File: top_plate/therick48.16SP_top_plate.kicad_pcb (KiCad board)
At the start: 2 copper layers, 313.1 x 75.2 mm, 85 parts, among them U1 HOLE, U10 HOLE, U11 HOLE, U12 HOLE, U13 HOLE, U14 HOLE, U15 HOLE, U16 HOLE, U17 HOLE, U18 HOLE, U19 HOLE, U2 HOLE, U20 HOLE, U21 HOLE, U22 HOLE, U23 HOLE, U24 HOLE, U25 HOLE, U26 HOLE, U27 HOLE, U28 HOLE, U29 HOLE, U3 HOLE, U30 HOLE, U31 HOLE, U32 HOLE, U33 HOLE, U34 HOLE, U35 HOLE, U36 HOLE, U37 HOLE, U38 HOLE, U39 HOLE, U4 HOLE, U40 HOLE, U41 HOLE, U42 HOLE, U43 HOLE, U44 HOLE, U45 HOLE, U46 HOLE, U47 HOLE, U48 HOLE, U49 HOLE, U5 HOLE, U50 HOLE, U51 HOLE, U52 HOLE, U53 HOLE, U54 HOLE, U55 HOLE, U56 HOLE, U57 HOLE, U58 HOLE, U59 HOLE, U6 HOLE, U60 HOLE, U61 HOLE, U62 HOLE, U63 HOLE, U64 HOLE, U65 HOLE, U66 HOLE, U67 HOLE, U7 HOLE, U8 HOLE, U9 HOLE

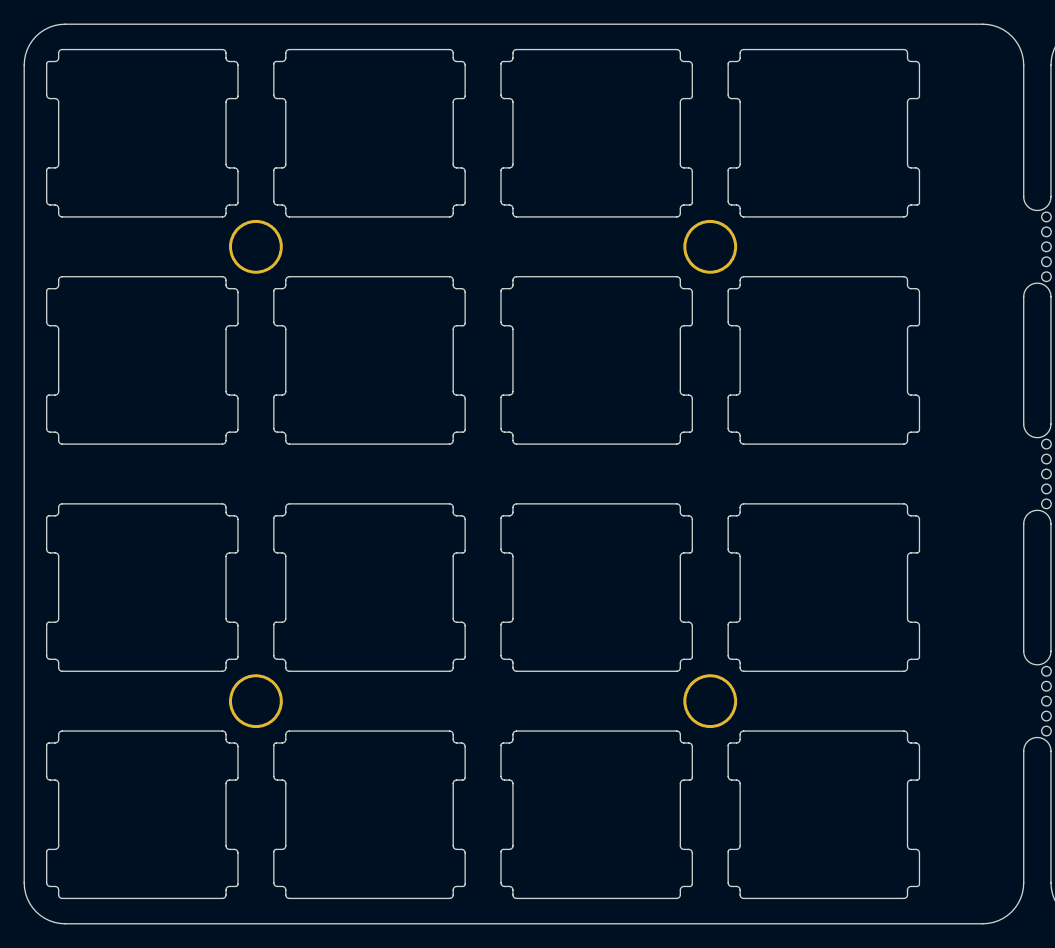
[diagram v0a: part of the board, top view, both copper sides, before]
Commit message: Changed gap between 4X12 and 4X4 to .25 inches
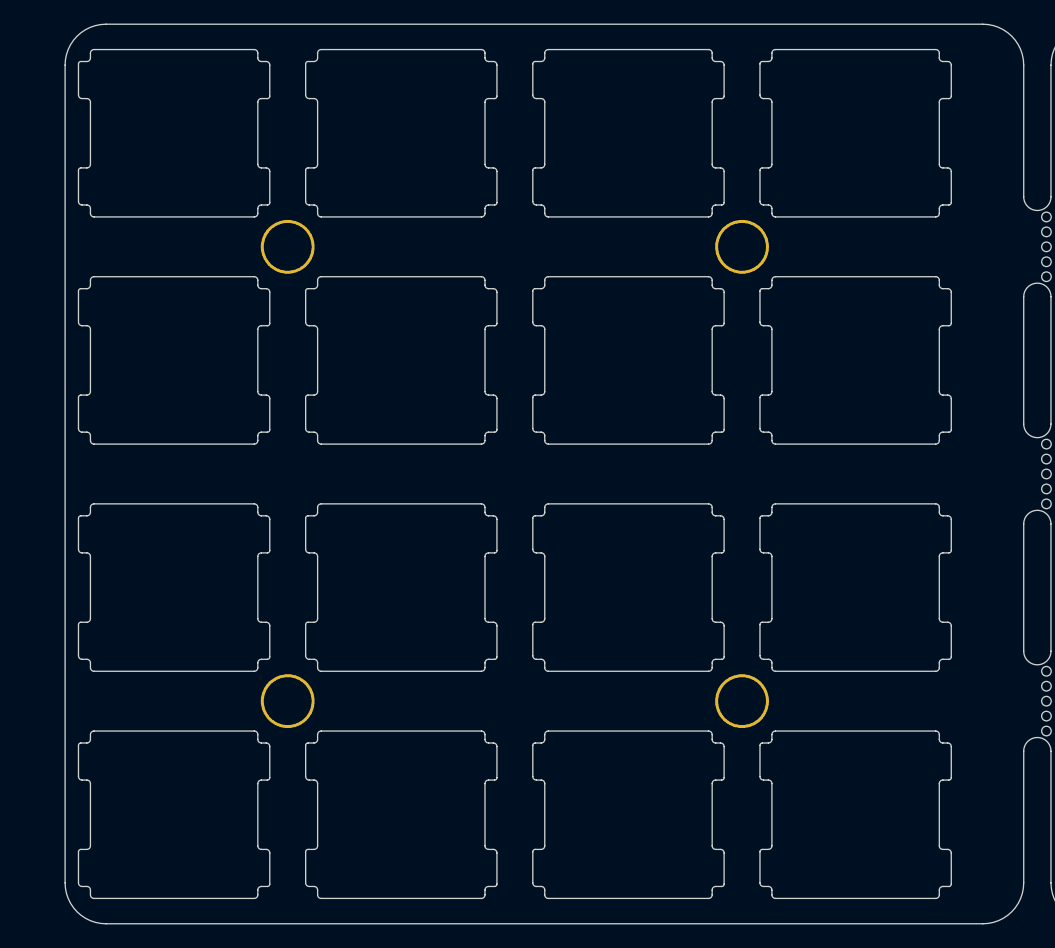
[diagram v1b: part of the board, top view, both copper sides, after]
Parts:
- moved H10 2.66 mm to (105.6, 101.2)
- moved H7 2.66 mm to (67.6, 63.2)
- moved H8 2.66 mm to (105.6, 63.2)
- moved H9 2.66 mm to (67.6, 101.2)
- moved U49 2.66 mm to (58.1, 51.7)
- moved U50 2.66 mm to (77.1, 51.7)
- moved U51 2.66 mm to (96.1, 51.7)
- moved U52 2.66 mm to (115.1, 51.7)
- moved U53 2.66 mm to (58.1, 70.7)
- moved U54 2.66 mm to (77.1, 70.7)
- moved U55 2.66 mm to (96.1, 70.7)
- moved U56 2.66 mm to (115.1, 70.7)
- moved U57 2.66 mm to (58.1, 89.7)
- moved U58 2.66 mm to (77.1, 89.7)
- moved U59 2.66 mm to (96.1, 89.7)
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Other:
- board size 313.1 x 75.2 mm -> 309.7 x 75.2 mm
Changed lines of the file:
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@@
   (general
     (thickness 1.6)
-    (drawings 30)
+    (drawings 31)
     (tracks 0)
     (zones 0)
@@
   )
   (module random-keyboard-parts:plate_hole_4mm_tht locked (layer F.Cu)
-    (at 102.9292 101.212)
+    (at 105.589193 101.212)
     (fp_text reference H10 (at 0.381 1.4097) (layer Dwgs.User)
       (effects (font (size 1 1) (thickness 0.15)))
@@
   )
   (module random-keyboard-parts:plate_hole_4mm_tht locked (layer F.Cu)
-    (at 64.9292 101.212)
+    (at 67.589193 101.212)
     (fp_text reference H9 (at 0.381 1.4097) (layer Dwgs.User)
       (effects (font (size 1 1) (thickness 0.15)))
@@
   )
   (module random-keyboard-parts:plate_hole_4mm_tht locked (layer F.Cu)
-    (at 102.9292 63.212)
+    (at 105.589193 63.212)
     (fp_text reference H8 (at 0.381 1.4097) (layer Dwgs.User)
       (effects (font (size 1 1) (thickness 0.15)))
@@
   )
   (module random-keyboard-parts:plate_hole_4mm_tht locked (layer F.Cu)
-    (at 64.9292 63.212)
+    (at 67.589193 63.212)
     (fp_text reference H7 (at 0.381 1.4097) (layer Dwgs.User)
       (effects (font (size 1 1) (thickness 0.15)))
@@
   )
   (module random-keyboard-parts:MX100_slot (layer F.Cu)
-    (at 112.479704 108.679714)
+    (at 115.139697 108.679714)
     (fp_text reference U64 (at 0.0127 1.8288) (layer Dwgs.User)
       (effects (font (size 1 1) (thickness 0.15)))
@@
   )
   (module random-keyboard-parts:MX100_slot (layer F.Cu)
-    (at 93.479754 108.679714)
+    (at 96.139747 108.679714)
     (fp_text reference U63 (at 0.0127 1.8288) (layer Dwgs.User)
       (effects (font (size 1 1) (thickness 0.15)))
@@
   )
   (module random-keyboard-parts:MX100_slot (layer F.Cu)
-    (at 74.479804 108.679714)
+    (at 77.139797 108.679714)
     (fp_text reference U62 (at 0.0127 1.8288) (layer Dwgs.User)
       (effects (font (size 1 1) (thickness 0.15)))
@@
   )
   (module random-keyboard-parts:MX100_slot (layer F.Cu)
-    (at 55.479854 108.679714)
+    (at 58.139847 108.679714)
     (fp_text reference U61 (at 0.0127 1.8288) (layer Dwgs.User)
       (effects (font (size 1 1) (thickness 0.15)))
@@
   )
   (module random-keyboard-parts:MX100_slot (layer F.Cu)
-    (at 112.479704 89.679764)
+    (at 115.139697 89.679764)
     (fp_text reference U60 (at 0.0127 1.8288) (layer Dwgs.User)
       (effects (font (size 1 1) (thickness 0.15)))
@@
   )
   (module random-keyboard-parts:MX100_slot (layer F.Cu)
-    (at 93.479754 89.679764)
+    (at 96.139747 89.679764)
     (fp_text reference U59 (at 0.0127 1.8288) (layer Dwgs.User)
       (effects (font (size 1 1) (thickness 0.15)))
@@
   )
   (module random-keyboard-parts:MX100_slot (layer F.Cu)
-    (at 74.479804 89.679764)
+    (at 77.139797 89.679764)
     (fp_text reference U58 (at 0.0127 1.8288) (layer Dwgs.User)
       (effects (font (size 1 1) (thickness 0.15)))
@@
   )
   (module random-keyboard-parts:MX100_slot (layer F.Cu)
-    (at 55.479854 89.679764)
+    (at 58.139847 89.679764)
     (fp_text reference U57 (at 0.0127 1.8288) (layer Dwgs.User)
       (effects (font (size 1 1) (thickness 0.15)))
@@
   )
   (module random-keyboard-parts:MX100_slot (layer F.Cu)
-    (at 112.479704 70.679814)
+    (at 115.139697 70.679814)
     (fp_text reference U56 (at 0.0127 1.8288) (layer Dwgs.User)
       (effects (font (size 1 1) (thickness 0.15)))
@@
   )
   (module random-keyboard-parts:MX100_slot (layer F.Cu)
-    (at 93.479754 70.679814)
+    (at 96.139747 70.679814)
     (fp_text reference U55 (at 0.0127 1.8288) (layer Dwgs.User)
       (effects (font (size 1 1) (thickness 0.15)))
@@
   )
   (module random-keyboard-parts:MX100_slot (layer F.Cu)
-    (at 74.479804 70.679814)
+    (at 77.139797 70.679814)
     (fp_text reference U54 (at 0.0127 1.8288) (layer Dwgs.User)
       (effects (font (size 1 1) (thickness 0.15)))
@@
   )
   (module random-keyboard-parts:MX100_slot (layer F.Cu)
-    (at 55.479854 70.679814)
+    (at 58.139847 70.679814)
     (fp_text reference U53 (at 0.0127 1.8288) (layer Dwgs.User)
       (effects (font (size 1 1) (thickness 0.15)))
@@
   )
   (module random-keyboard-parts:MX100_slot (layer F.Cu)
-    (at 112.479704 51.679864)
+    (at 115.139697 51.679864)
     (fp_text reference U52 (at 0.0127 1.8288) (layer Dwgs.User)
       (effects (font (size 1 1) (thickness 0.15)))
@@
   )
   (module random-keyboard-parts:MX100_slot (layer F.Cu)
-    (at 93.479754 51.679864)
+    (at 96.139747 51.679864)
     (fp_text reference U51 (at 0.0127 1.8288) (layer Dwgs.User)
       (effects (font (size 1 1) (thickness 0.15)))
@@
   )
   (module random-keyboard-parts:MX100_slot (layer F.Cu)
-    (at 74.479804 51.679864)
+    (at 77.139797 51.679864)
     (fp_text reference U50 (at 0.0127 1.8288) (layer Dwgs.User)
       (effects (font (size 1 1) (thickness 0.15)))
@@
   )
   (module random-keyboard-parts:MX100_slot (layer F.Cu)
-    (at 55.479854 51.679864)
+    (at 58.139847 51.679864)
     (fp_text reference U49 (at 0.0127 1.8288) (layer Dwgs.User)
       (effects (font (size 1 1) (thickness 0.15)))
@@
     (fp_arc (start -7.8 -5.8) (end -7.8 -6) (angle -90) (layer Edge.Cuts) (width 0.1))
   )
+  (dimension 6.409933 (width 0.15) (layer Dwgs.User)
+    (gr_text "0.2524 in" (at 127.869663 37.079899) (layer Dwgs.User)
+      (effects (font (size 1 1) (thickness 0.15)))
+    )
+    (feature1 (pts (xy 124.664697 42.154864) (xy 124.664697 37.793478)))
+    (feature2 (pts (xy 131.07463 42.154864) (xy 131.07463 37.793478)))
+    (crossbar (pts (xy 131.07463 38.379899) (xy 124.664697 38.379899)))
+    (arrow1a (pts (xy 124.664697 38.379899) (xy 125.791201 37.793478)))
+    (arrow1b (pts (xy 124.664697 38.379899) (xy 125.791201 38.96632)))
+    (arrow2a (pts (xy 131.07463 38.379899) (xy 129.948126 37.793478)))
+    (arrow2b (pts (xy 131.07463 38.379899) (xy 129.948126 38.96632)))
+  )
   (gr_line (start 358.72 114.38) (end 358.72 45.98) (layer Edge.Cuts) (width 0.05))
   (gr_arc (start 130.34 57) (end 129.2 57) (angle -180) (layer Edge.Cuts) (width 0.05))
@@
   (gr_line (start 129.2 45.98) (end 129.2 57) (layer Edge.Cuts) (width 0.05))
   (gr_line (start 131.48 45.98) (end 131.48 57) (layer Edge.Cuts) (width 0.05))
-  (gr_line (start 125.78 42.56) (end 49.02 42.56) (layer Edge.Cuts) (width 0.05))
-  (gr_line (start 45.6 114.38) (end 45.6 45.98) (layer Edge.Cuts) (width 0.05))
-  (gr_line (start 49.02 117.8) (end 125.78 117.8) (layer Edge.Cuts) (width 0.05))
-  (gr_arc (start 49.02 114.38) (end 45.6 114.38) (angle -90) (layer Edge.Cuts) (width 0.05))
-  (gr_arc (start 49.02 45.98) (end 49.02 42.56) (angle -90) (layer Edge.Cuts) (width 0.05))
+  (gr_line (start 125.78 42.56) (end 52.439991 42.56) (layer Edge.Cuts) (width 0.05))
+  (gr_line (start 49.019991 114.38) (end 49.019991 45.98) (layer Edge.Cuts) (width 0.05))
+  (gr_line (start 52.439991 117.8) (end 125.78 117.8) (layer Edge.Cuts) (width 0.05))
+  (gr_arc (start 52.439991 114.38) (end 49.019991 114.38) (angle -90) (layer Edge.Cuts) (width 0.05))
+  (gr_arc (start 52.439991 45.98) (end 52.439991 42.56) (angle -90) (layer Edge.Cuts) (width 0.05))
   (gr_arc (start 125.78 45.98) (end 129.2 45.98) (angle -90) (layer Edge.Cuts) (width 0.05))
   (gr_arc (start 125.78 114.38) (end 125.78 117.8) (angle -90) (layer Edge.Cuts) (width 0.05))

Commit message: 48+16SP to 48.16SP
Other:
- board text added: "therick48.16SP Rev 1.0"
- board text removed: "therick48+16SP Rev 1.0"
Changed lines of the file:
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@@
   (gr_arc (start 130.34 95) (end 129.2 95) (angle -180) (layer Edge.Cuts) (width 0.05))
   (gr_arc (start 130.34 103.36) (end 131.48 103.36) (angle -180) (layer Edge.Cuts) (width 0.05))
-  (gr_text "therick48+16SP Rev 1.0" (at 321.48 99.18) (layer B.SilkS)
+  (gr_text "therick48.16SP Rev 1.0" (at 245.099355 99.179739) (layer B.SilkS)
     (effects (font (size 1.5 1.5) (thickness 0.2)) (justify mirror))
   )
